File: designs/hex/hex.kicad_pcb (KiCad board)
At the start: 2 copper layers, 50 x 50 mm, 33 parts, among them IC1 ATMEGA1284P-P, K1 RESONATOR, K2 REGUL, K3 ANALOG, P1 PROG, P2 XBEE, P3 BATT (4.8V-6V), P4 DPDT, P5 I2C, P6 BATT (4.8V-6V)

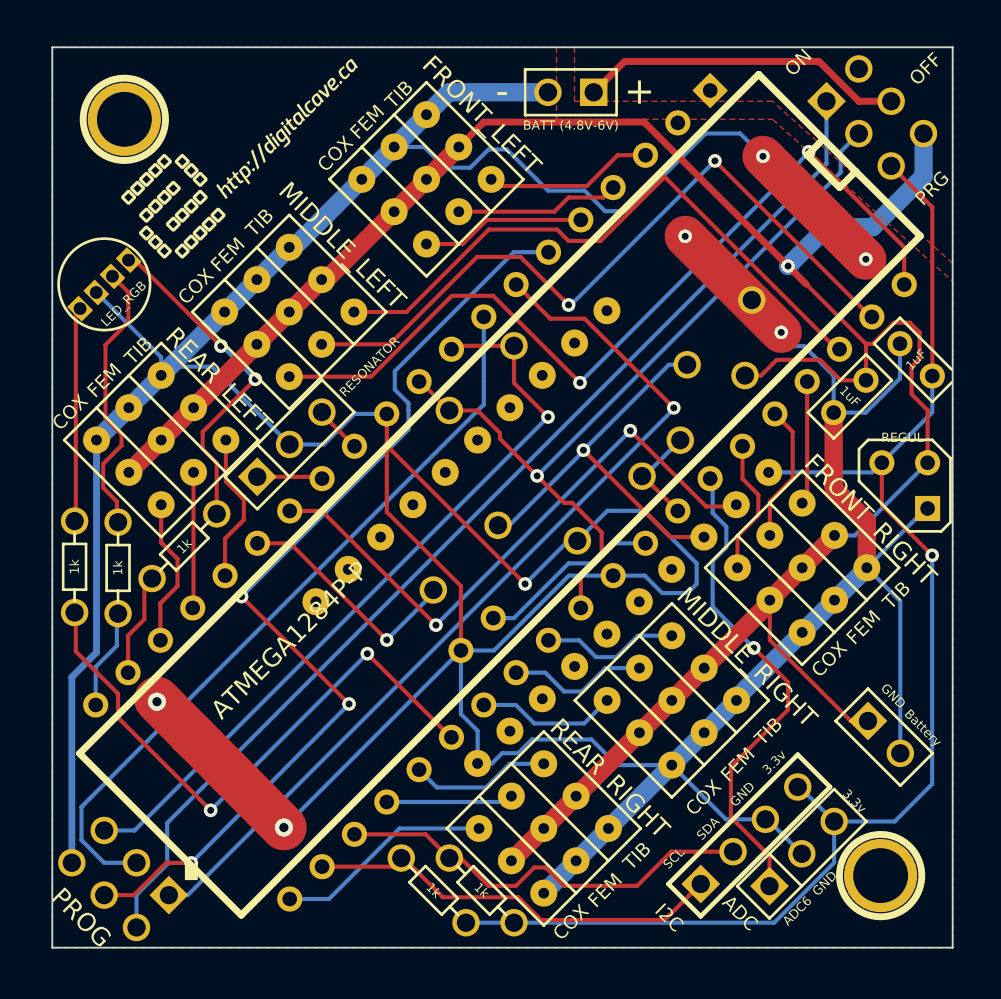
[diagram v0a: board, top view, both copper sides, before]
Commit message: Layout improvements and change to consolidated expansion header
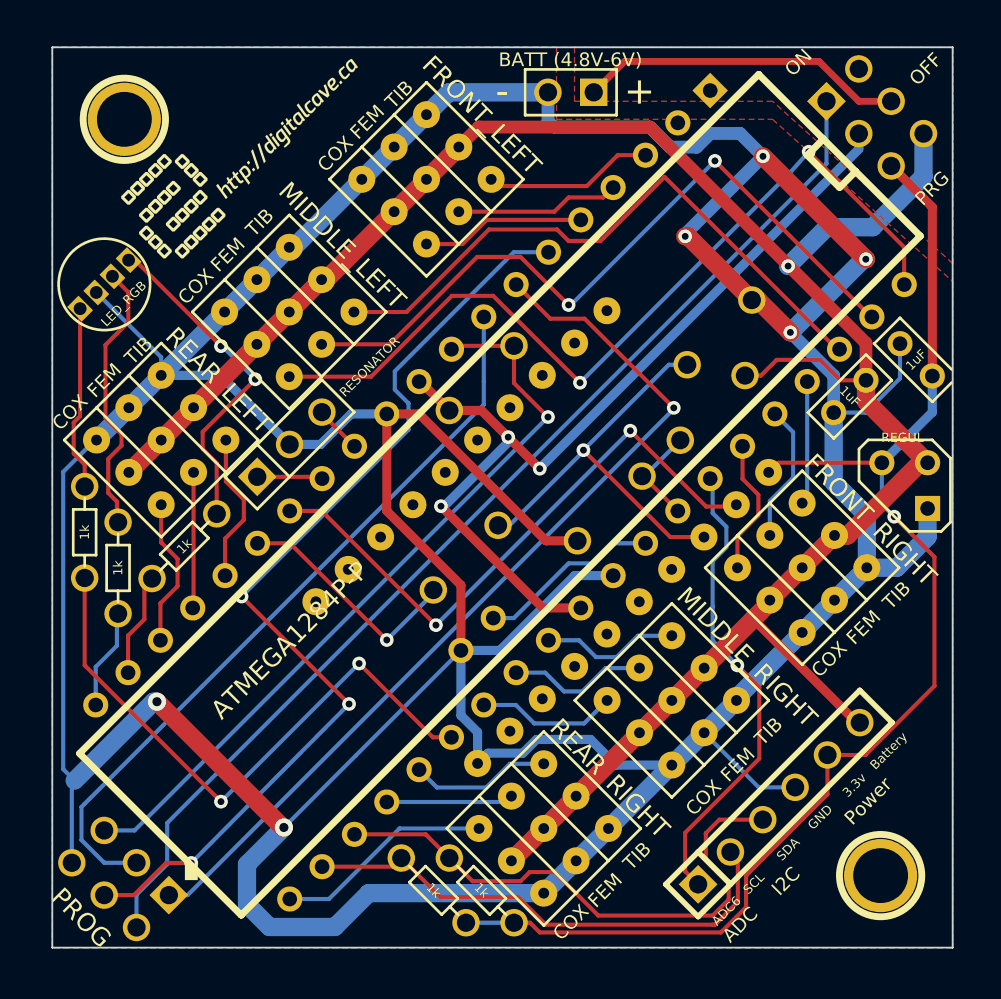
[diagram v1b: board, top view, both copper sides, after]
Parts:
- removed K3: ANALOG, PIN_ARRAY_3X1
- removed P6: BATT (4.8V-6V), PIN_ARRAY_2X1
- P5: value I2C -> CONN_6; footprint PIN_ARRAY_4x1 -> PIN_ARRAY-6X1
- moved P5 2.43 mm to (165.4, 87.0)
- moved R4 2.00 mm to (126.8, 71.9)
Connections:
- net N-0000027 renamed RESONATOR_2
- net N-0000028 renamed RESONATOR_1
- net N-0000033 renamed AREF
- C3 pad 1: VCC_XBEE -> VCC_3v3
- K2 pad 3: VCC_XBEE -> VCC_3v3
- P2 pad 1: VCC_XBEE -> VCC_3v3
- P4 pad 6: VCC_XBEE -> VCC_3v3
- P5 pad 1: I2C_SCL -> ADC6
- P5 pad 2: I2C_SDA -> I2C_SCL
- P5 pad 3: GND -> I2C_SDA
- P5 pad 4: VCC_XBEE -> GND
- R7 pad 1: VCC_XBEE -> VCC_3v3
- R8 pad 1: VCC_XBEE -> VCC_3v3
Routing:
- net VCC_XBEE: track 77.3 -> 0.00 mm, vias 1 -> 0
- net VCC_3v3: track 0.00 -> 72.9 mm, vias 0 -> 1
- net I2C_SDA: track 23.8 -> 31.1 mm
- net SWITCHED_BATTERY: track 154.4 -> 147.6 mm
- net VCC_AVR: track 44.9 -> 50.2 mm, vias 1 -> 3
- net I2C_SCL: track 23.5 -> 28.3 mm
- net GND: track 295.6 -> 297.8 mm, vias 7 -> 6
- net LED_RED_R: track 12.0 -> 10.3 mm
- net ADC6: track 27.3 -> 26.3 mm
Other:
- board text added: "Power"

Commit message: Added a breakout for port B0 for debugging output
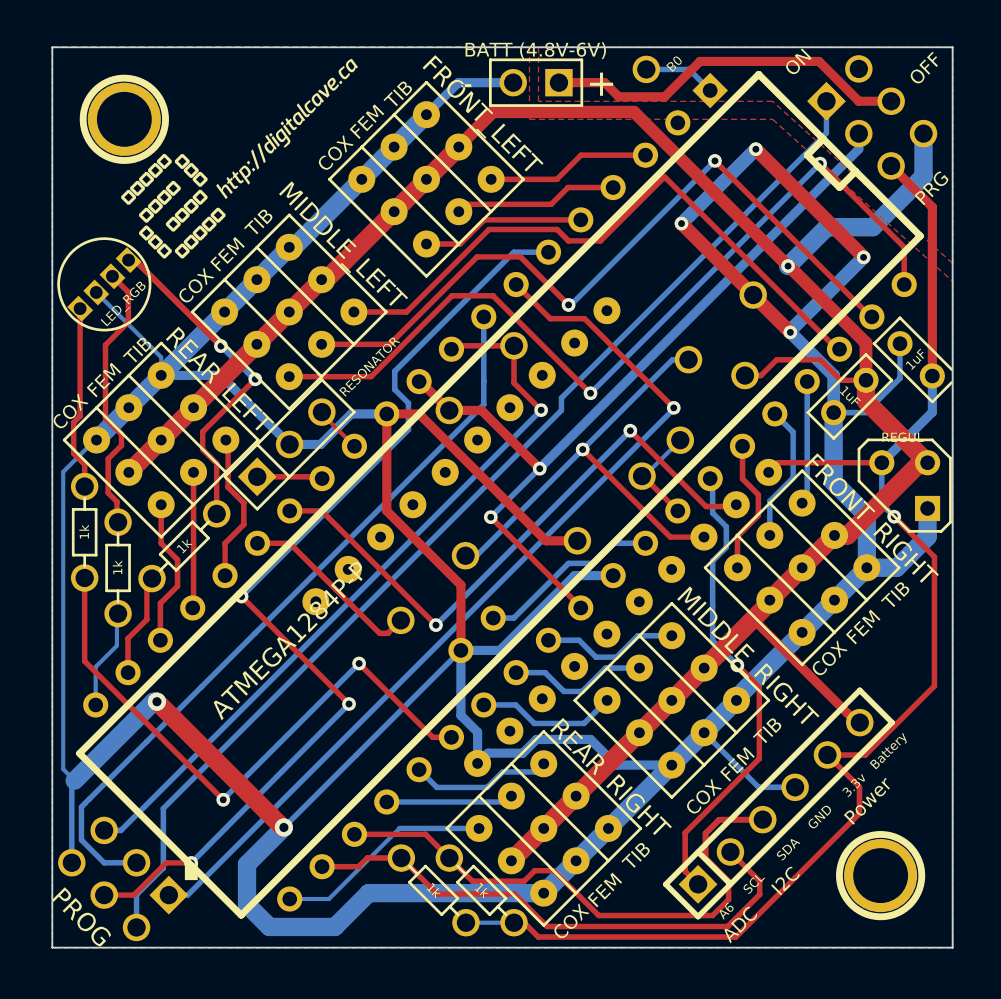
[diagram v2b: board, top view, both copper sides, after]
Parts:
- added P6: CONN_1, PIN_ARRAY_1, F.Cu at (158.0, 46.2)
- moved R9 2.47 mm to (146.2, 75.0)
- moved P3 2.00 mm to (151.9, 47.0)
- moved D1 0.29 mm to (162.1, 60.6)
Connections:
- IC1 pad 1: (no net) -> N-0000019
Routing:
- net GND: track 297.8 -> 279.8 mm
- net LED_GREEN_R: track 18.8 -> 29.7 mm
- net I2C_SDA: track 31.1 -> 40.2 mm
- net LED_RED: track 33.2 -> 38.8 mm
- net VCC_AVR: track 50.2 -> 45.6 mm, vias 3 -> 2
- net N-0000019: track 0.00 -> 4.03 mm
- net PWM12: track 8.30 -> 11.7 mm
- net N-0000018: track 13.3 -> 10.3 mm, vias 1 -> 0
- net AVR_TX: track 22.9 -> 25.6 mm
- net BATTERY: track 18.1 -> 20.5 mm
- net VCC_3v3: track 72.9 -> 75.2 mm
- net VCC_PROG: track 61.8 -> 63.6 mm
- net I2C_SCL: track 28.3 -> 29.9 mm
- net RESET: track 42.4 -> 41.7 mm
- net SWITCHED_BATTERY: track 147.6 -> 148.2 mm
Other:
- net class Default: trace_width 0.2286 -> 0.3048
- rule trace_min: 0.2032 -> 0.2286
- board text added: "A6"
- board text added: "B0"
- board text removed: "ADC6"

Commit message: Added some more labels to XBee, and cleaned up the servo labels
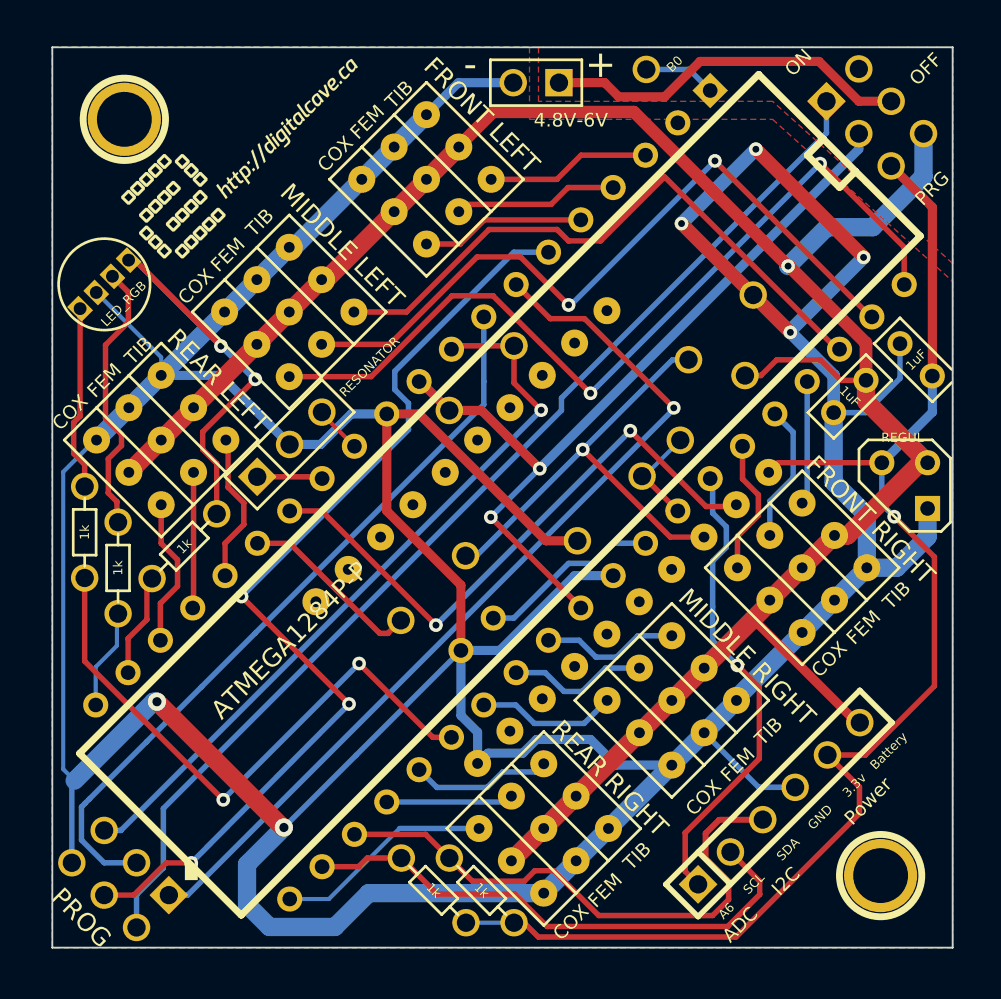
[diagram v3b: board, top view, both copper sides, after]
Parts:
- P3: value BATT (4.8V-6V) -> 4.8V-6V
- S1: value FRONT_LEFT -> FRONT LEFT
- S2: value FRONT_RIGHT -> FRONT RIGHT
- S3: value MIDDLE_LEFT -> MIDDLE LEFT
- S4: value MIDDLE_RIGHT -> MIDDLE RIGHT
- S5: value REAR_LEFT -> REAR LEFT
- S6: value REAR_RIGHT -> REAR RIGHT
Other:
- board text added: "RX"
- board text added: "TX"
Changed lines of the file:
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@@
     (area 113.714287 39.150001 188 102.7)
     (thickness 1.6)
-    (drawings 24)
+    (drawings 28)
     (tracks 459)
     (zones 0)
@@
       (effects (font (size 1 1) (thickness 0.15)))
     )
-    (fp_text value MIDDLE_RIGHT (at 1.885854 -6.555587 315) (layer F.SilkS)
+    (fp_text value "MIDDLE RIGHT" (at 1.885854 -6.555587 315) (layer F.SilkS)
       (effects (font (size 1 1) (thickness 0.15)))
     )
@@
       (effects (font (size 1 1) (thickness 0.15)))
     )
-    (fp_text value MIDDLE_LEFT (at 1.167433 2.783879 135) (layer F.SilkS)
+    (fp_text value "MIDDLE LEFT" (at 1.167433 2.783879 135) (layer F.SilkS)
       (effects (font (size 1 1) (thickness 0.15)))
     )
@@
       (effects (font (size 1 1) (thickness 0.15)))
     )
-    (fp_text value FRONT_LEFT (at 0.987828 2.783879 135) (layer F.SilkS)
+    (fp_text value "FRONT LEFT" (at 0.987828 2.783879 135) (layer F.SilkS)
       (effects (font (size 1 1) (thickness 0.15)))
     )
@@
       (effects (font (size 0.762 0.762) (thickness 0.1524)))
     )
-    (fp_text value "BATT (4.8V-6V)" (at 0.0254 1.8034 180) (layer F.SilkS)
+    (fp_text value 4.8V-6V (at -1.9304 -2.0828 180) (layer F.SilkS)
       (effects (font (size 0.762 0.762) (thickness 0.127)))
     )
@@
       (effects (font (size 1 1) (thickness 0.15)))
     )
-    (fp_text value REAR_LEFT (at 0.71842 2.694077 135) (layer F.SilkS)
+    (fp_text value "REAR LEFT" (at 0.71842 2.694077 135) (layer F.SilkS)
       (effects (font (size 1 1) (thickness 0.15)))
     )
@@
       (effects (font (size 1 1) (thickness 0.15)))
     )
-    (fp_text value FRONT_RIGHT (at 1.436841 -6.465784 315) (layer F.SilkS)
+    (fp_text value "FRONT RIGHT" (at 1.436841 -6.465784 315) (layer F.SilkS)
       (effects (font (size 1 1) (thickness 0.15)))
     )
@@
       (effects (font (size 1 1) (thickness 0.15)))
     )
-    (fp_text value REAR_RIGHT (at 1.257236 -6.465784 315) (layer F.SilkS)
+    (fp_text value "REAR RIGHT" (at 1.257236 -6.465784 315) (layer F.SilkS)
       (effects (font (size 1 1) (thickness 0.15)))
     )
@@
       (effects (font (size 1 1) (thickness 0.15)) (justify mirror))
     )
-    (fp_text value "3.3v ZENER" (at -0.044901 1.661347 225) (layer B.SilkS)
+    (fp_text value "3.3v ZENER" (at -0.790263 -0.143684 315) (layer B.SilkS)
       (effects (font (size 0.508 0.508) (thickness 0.127)) (justify mirror))
     )
@@
       (rotate (xyz 0 0 0))
     )
+  )
+  (gr_text GND (at 150.3426 84.7852) (layer B.SilkS)
+    (effects (font (size 0.508 0.508) (thickness 0.127)) (justify mirror))
+  )
+  (gr_text TX (at 164.5412 70.4596) (layer B.SilkS)
+    (effects (font (size 0.508 0.508) (thickness 0.127)) (justify mirror))
+  )
+  (gr_text 3.3v (at 166.7002 68.5292) (layer B.SilkS)
+    (effects (font (size 0.508 0.508) (thickness 0.127)) (justify mirror))
+  )
+  (gr_text RX (at 162.7886 72.2376) (layer B.SilkS)
+    (effects (font (size 0.508 0.508) (thickness 0.127)) (justify mirror))
   )
   (gr_text B0 (at 159.5374 45.8978 225) (layer F.SilkS)
@@
     (effects (font (size 5.08 5.08) (thickness 1.27)) (justify mirror))
   )
-  (gr_text - (at 148 47) (layer F.SilkS)
+  (gr_text - (at 148.209 45.9486) (layer F.SilkS)
     (effects (font (size 1.5 1.5) (thickness 0.3)) (justify mirror))
   )
-  (gr_text + (at 155.5 47) (layer F.SilkS)
+  (gr_text + (at 155.448 45.9486) (layer F.SilkS)
     (effects (font (size 1.5 1.5) (thickness 0.3)) (justify mirror))
   )

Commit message: Improved power routing and zone definitions.
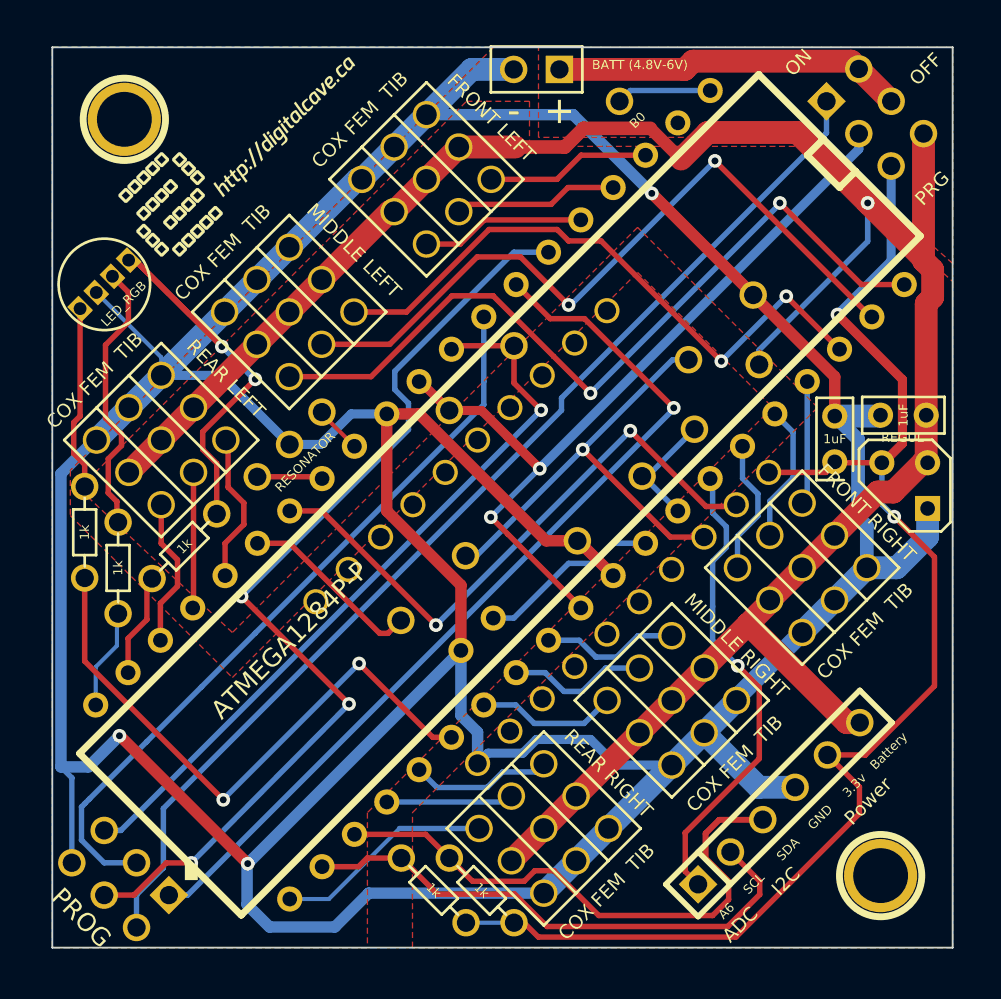
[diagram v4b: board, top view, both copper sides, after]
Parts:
- P3: value 4.8V-6V -> BATT (4.8V-6V)
- S2, S4, S6: footprint HEX_LEG -> HEX_LEG_REVERSE
- moved C3 6.30 mm to (168.5, 66.8), turned to 90 degrees
- moved C2 3.15 mm to (172.3, 65.4), turned to 0 degrees
- moved P6 2.31 mm to (156.5, 48.0)
- moved R2 1.00 mm to (162.5, 64.4)
- moved P3 0.74 mm to (151.9, 46.2)
- moved ? 0.18 mm to (135.2, 50.1)
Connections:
- P4 pad 1: (no net) -> BATTERY
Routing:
- net GND: track 279.8 -> 257.9 mm, vias 6 -> 3
- net SWITCHED_BATTERY: track 148.2 -> 127.2 mm
- net PWM06: track 47.6 -> 44.5 mm
- net BATTERY: track 20.5 -> 22.1 mm
- net N-0000018: track 4.03 -> 5.28 mm
- net VCC_3v3: track 75.2 -> 76.4 mm, vias 1 -> 2
- net ADC_BATTERY_METER: track 5.74 -> 6.78 mm
- net PWM08: vias 0 -> 2
- added copper zone on F.Cu, net GND

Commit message: Adjusting and verifying pin sizes
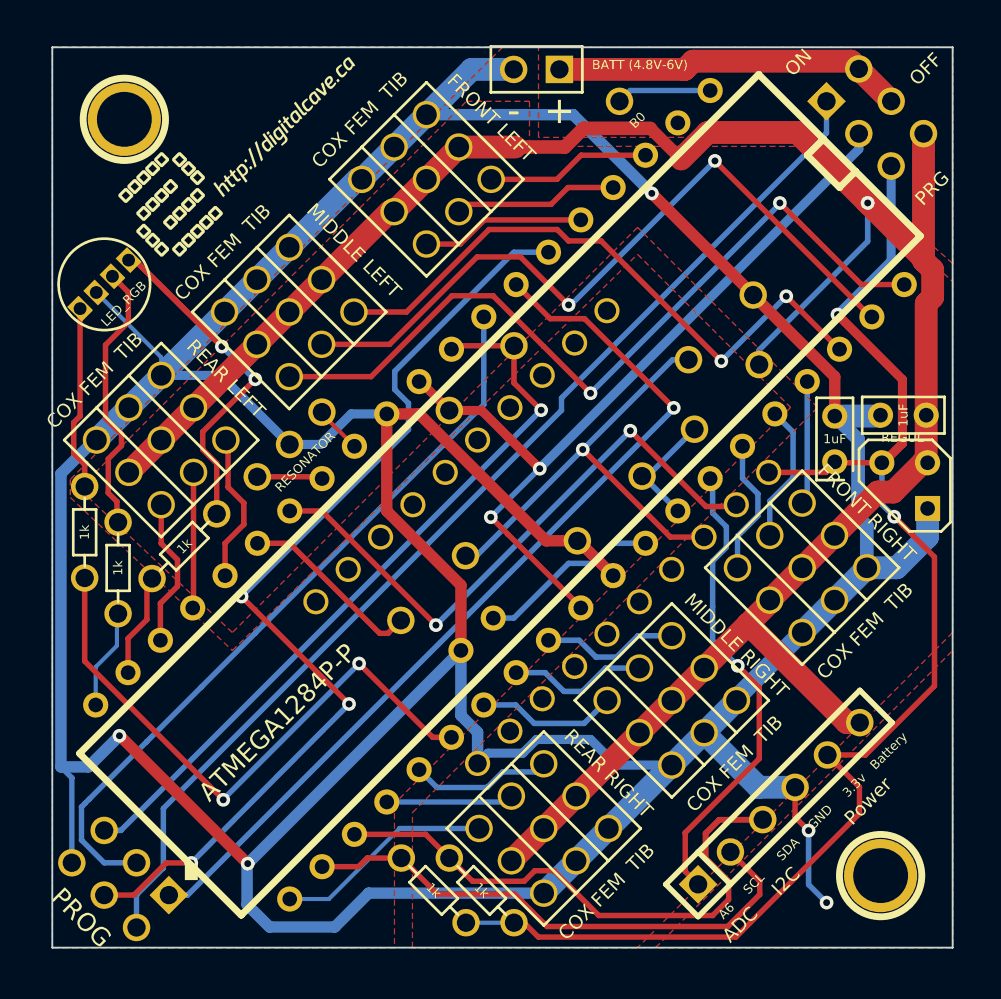
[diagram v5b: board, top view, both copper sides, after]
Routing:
- net GND: track 257.9 -> 265.0 mm, vias 3 -> 5
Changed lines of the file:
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@@
-(kicad_pcb (version 3) (host pcbnew "(2014-01-10 BZR 4027)-stable")
+(kicad_pcb (version 3) (host pcbnew "(2013-dec-23)-stable")
   (general
     (links 109)
@@
     (thickness 1.6)
     (drawings 28)
-    (tracks 448)
+    (tracks 454)
     (zones 0)
     (modules 32)
@@
   (layers
     (15 F.Cu signal)
-    (0 B.Cu signal hide)
+    (0 B.Cu signal)
     (16 B.Adhes user)
     (17 F.Adhes user)
@@
     (user_trace_width 1.27)
     (trace_clearance 0.2032)
-    (zone_clearance 0.381)
+    (zone_clearance 0.3302)
     (zone_45_only yes)
     (trace_min 0.2286)
@@
       (effects (font (size 1.778 1.143) (thickness 0.28575)))
     )
-    (fp_text value ATMEGA1284P-P (at 13.97 2.54 225) (layer F.SilkS)
+    (fp_text value ATMEGA1284P-P (at 17.684741 -0.205061 225) (layer F.SilkS)
       (effects (font (size 1.016 1.016) (thickness 0.254)))
     )
@@
   (segment (start 160.1216 46.228) (end 160.5788 45.7708) (width 1.27) (layer F.Cu) (net 6))
   (segment (start 169.789975 46.200923) (end 171.586026 47.996974) (width 1.016) (layer F.Cu) (net 6) (status 30))
+  (via (at 168 92.5) (size 0.762) (layers F.Cu B.Cu) (net 7))
+  (segment (start 168 92.5) (end 167 91.5) (width 0.3048) (layer B.Cu) (net 7))
+  (segment (start 166.252026 87.752026) (end 166.252026 86.096974) (width 0.3048) (layer F.Cu) (net 7))
+  (via (at 167 88.5) (size 0.762) (layers F.Cu B.Cu) (net 7))
+  (segment (start 166.252026 87.752026) (end 167 88.5) (width 0.3048) (layer F.Cu) (net 7))
+  (segment (start 167 88.5) (end 167 91.5) (width 0.3048) (layer B.Cu) (net 7))
   (segment (start 126.083923 90.287974) (end 126.083923 85.570923) (width 0.3048) (layer B.Cu) (net 7))
   (segment (start 126.083923 85.570923) (end 125.476 84.963) (width 0.3048) (layer B.Cu) (net 7))
@@
     (polygon
       (pts
-        (xy 175 95) (xy 145 95) (xy 145 87.5) (xy 167.5 65) (xy 157.5 55)
-        (xy 135 77.5) (xy 127 70) (xy 127 69) (xy 148 48) (xy 151.5 48)
-        (xy 151.5 50.5) (xy 166.5 50.5) (xy 175 58)
+        (xy 175 77.5) (xy 157.5 95) (xy 145 95) (xy 145 87.5) (xy 167.5 65)
+        (xy 157.5 55) (xy 135 77.5) (xy 127 70) (xy 127 69) (xy 148 48)
+        (xy 151.5 48) (xy 151.5 50.5) (xy 166.5 50.5) (xy 175 58)
       )
     )
@@
     (polygon
       (pts
-        (xy 165 65) (xy 142.5 87.5) (xy 142.5 95) (xy 125 95) (xy 125 70)
-        (xy 125 45) (xy 149.5 45) (xy 126 68.5) (xy 126 71) (xy 135 80)
-        (xy 157.5 57.5) (xy 165 65)
+        (xy 166 65) (xy 144 87) (xy 144 95) (xy 125 95) (xy 125 45)
+        (xy 150 45) (xy 126 69) (xy 126 70) (xy 135 78.5) (xy 157.5 56.5)
       )
     )
+  )
+  (zone (net 7) (net_name GND) (layer F.Cu) (hatch edge 0.508)
+    (connect_pads (clearance 0.3302))
+    (min_thickness 0.3302)
+    (fill (arc_segments 16) (thermal_gap 0.508) (thermal_bridge_width 0.508))
+    (polygon
+      (pts
+        (xy 175 78.5) (xy 175 95) (xy 158.5 95)
+      )
+    )
